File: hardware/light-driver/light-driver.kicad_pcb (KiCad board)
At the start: 2 copper layers, 59 x 18 mm, 62 parts, among them J1 LED-strip0, J2 Power/CAN, J3 LED-strip1, J4 Power/CAN, J5 SWD, J6 Conn_01x08_Pin, J7 ARGB, J8 Conn_01x04_Pin, Q1 IRLML0030, Q2 IRLML0030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

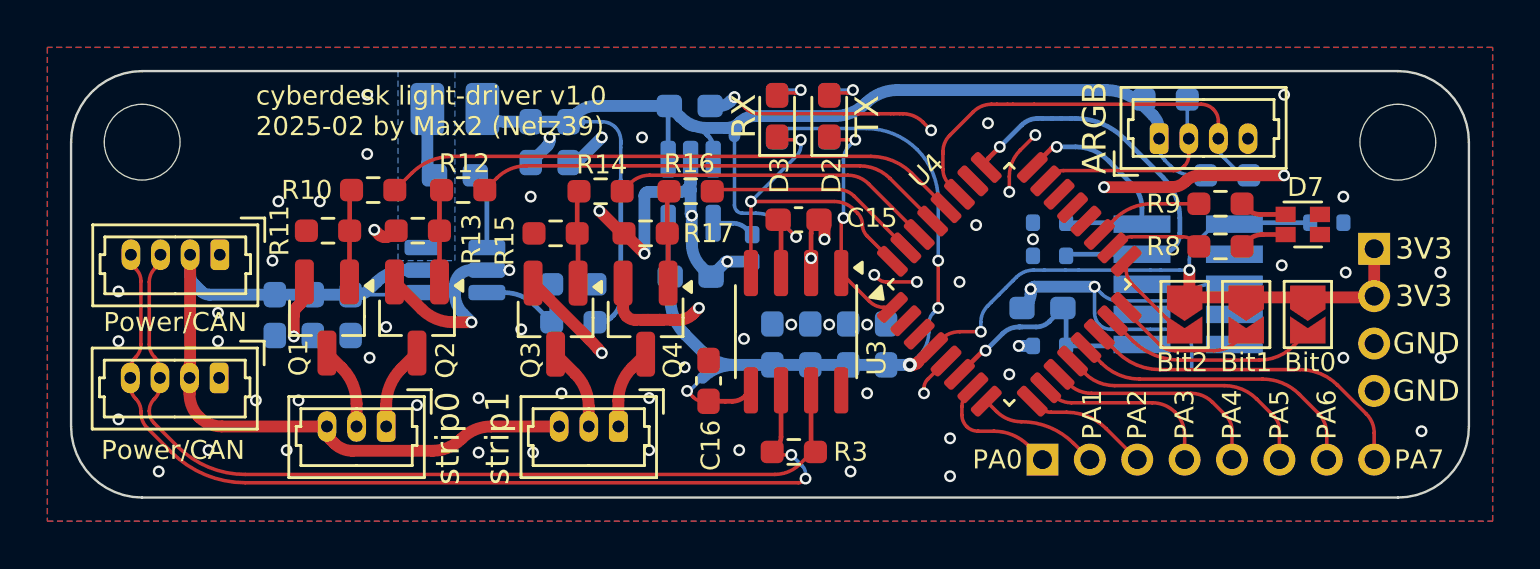
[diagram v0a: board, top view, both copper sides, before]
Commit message: Update footprints to given in inventory
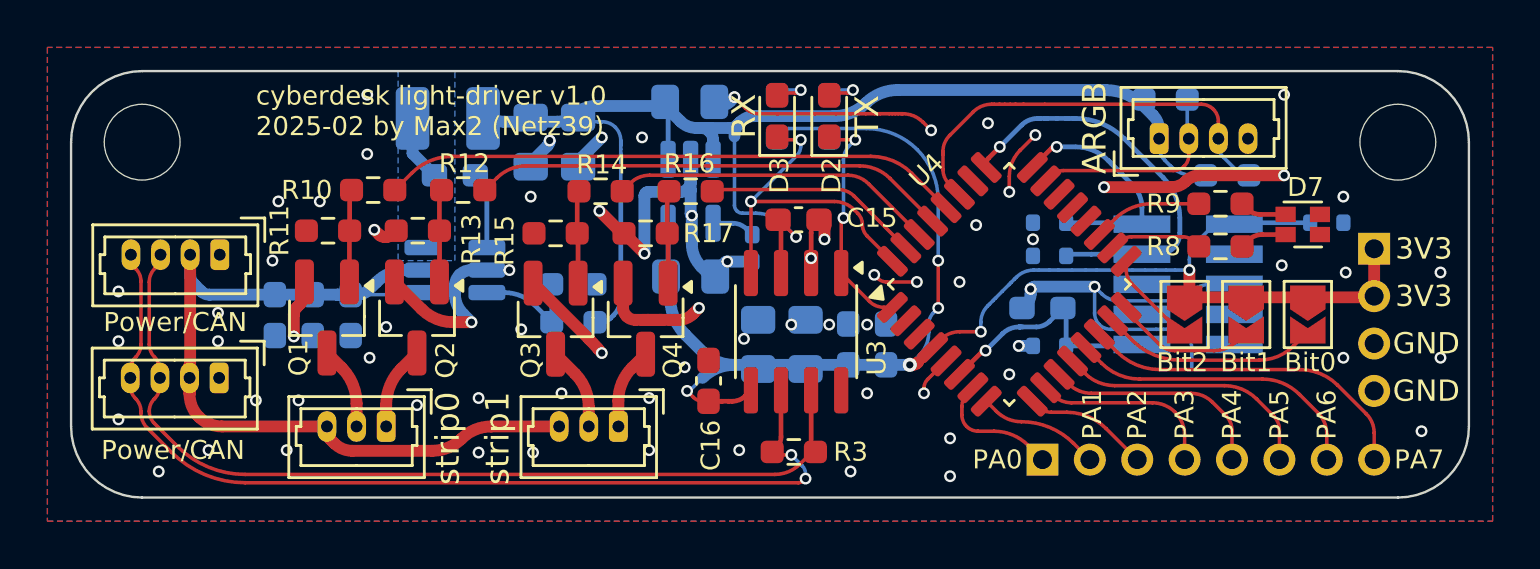
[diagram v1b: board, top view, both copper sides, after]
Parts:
- C11, C13, C2, C3, C4, C6: footprint Capacitor_SMD:C_0603_1608Metric_Pad1.08x0.95mm_HandSolder -> Capacitor_SMD:C_0805_2012Metric_Pad1.18x1.45mm_HandSolder
- L1: footprint Inductor_SMD:L_1008_2520Metric_Pad1.43x2.20mm_HandSolder -> Inductor_SMD:L_1210_3225Metric_Pad1.42x2.65mm_HandSolder
- moved C13 0.60 mm to (84.0, 102.5)
- moved L1 0.50 mm to (70.9, 93.0)
- moved C3 0.40 mm to (76.4, 94.0)
- moved C11 0.20 mm to (86.0, 102.5)
- moved C4 0.17 mm to (81.1, 92.3)
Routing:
- net +5V: track 61.5 -> 59.6 mm
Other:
- board text added: "Netz39 e.V."
- board text removed: "Netz39 e.V"
